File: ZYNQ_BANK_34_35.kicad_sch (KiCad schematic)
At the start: 16 parts, among them U1 XC7Z020-2CLG484I

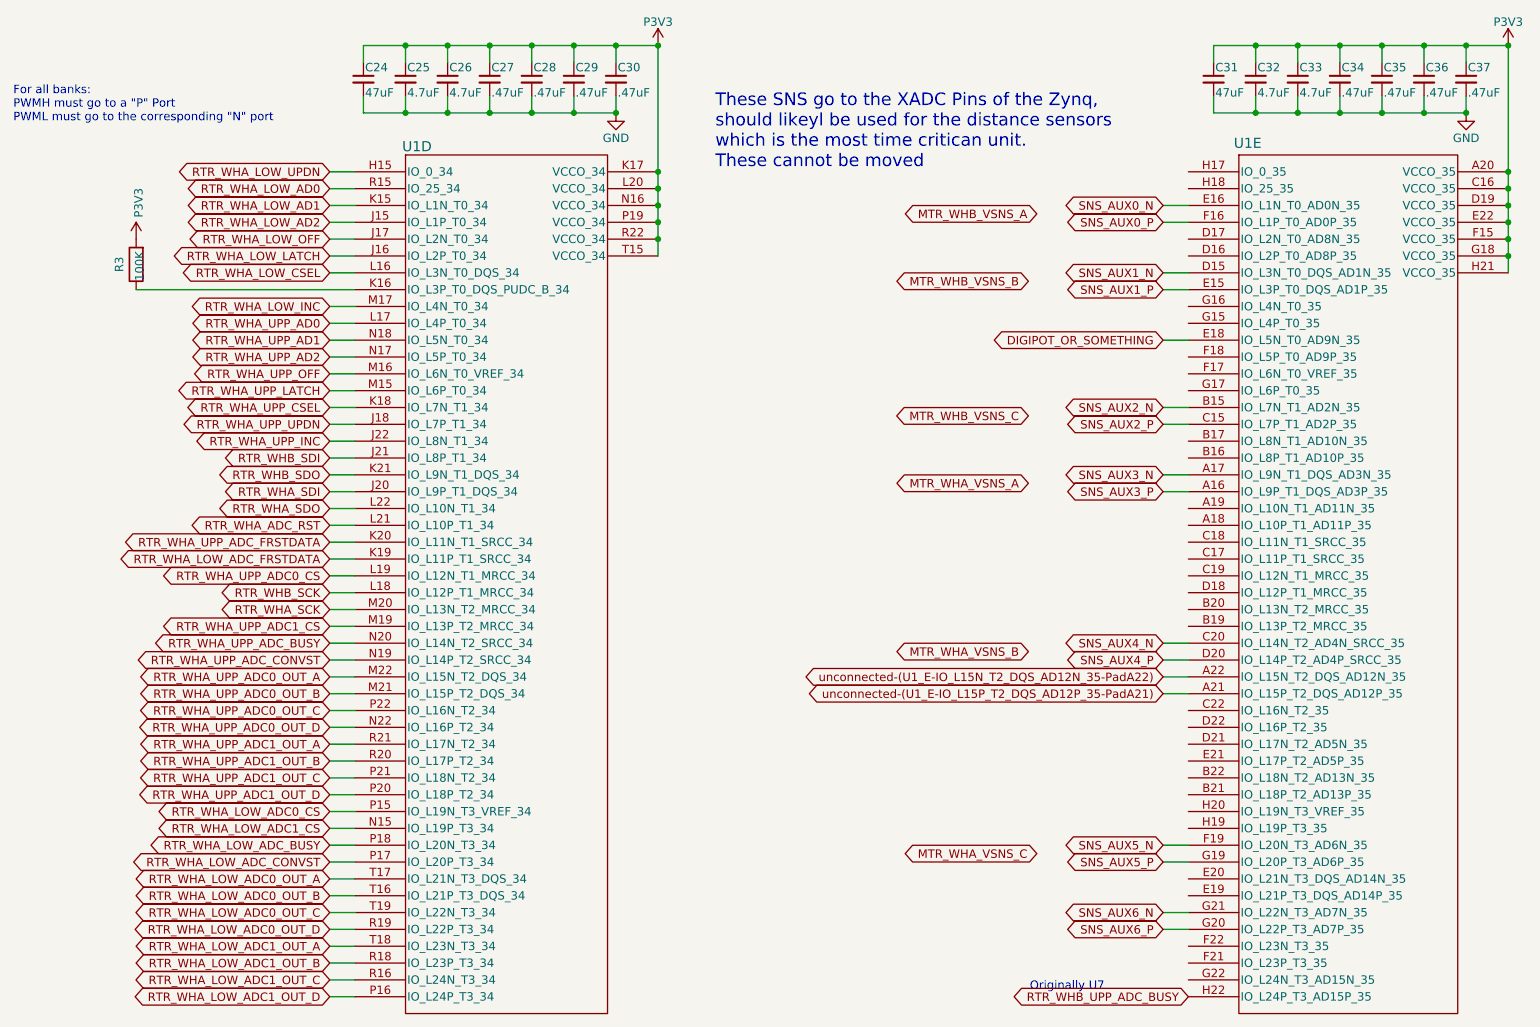
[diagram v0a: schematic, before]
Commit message: updated layouts, added motor
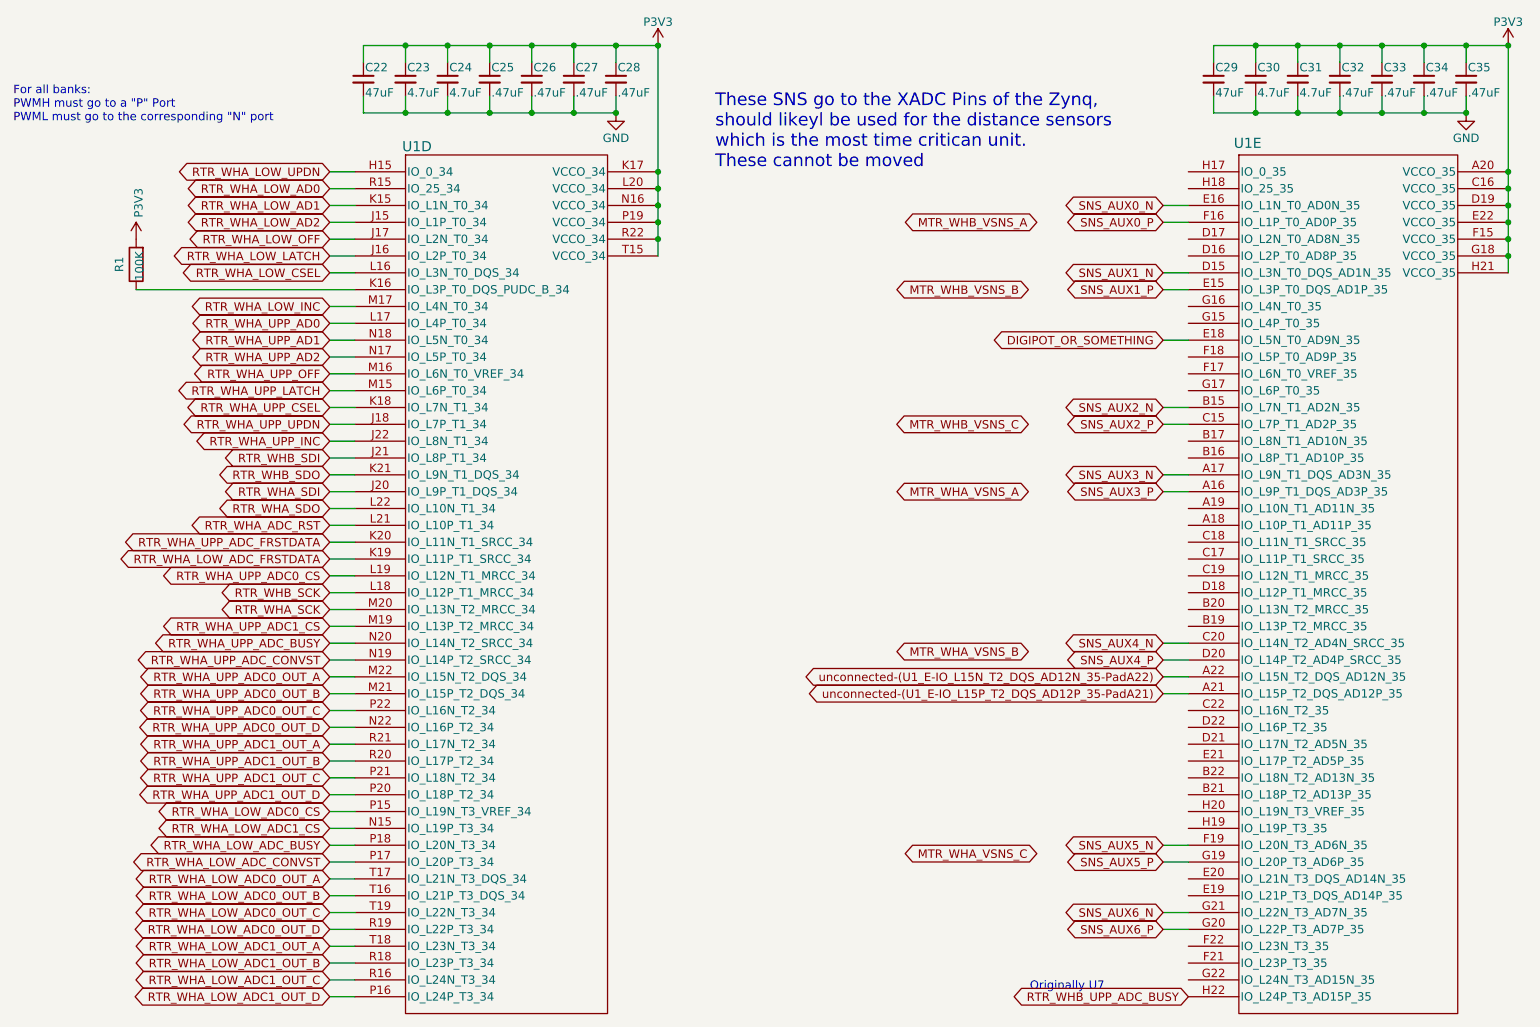
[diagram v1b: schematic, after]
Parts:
- renumbered C24 to C22, C25 to C23, C26 to C24, C27 to C25, C28 to C26, C29 to C27, C30 to C28, C31 to C29, C32 to C30, C33 to C31, C34 to C32, C35 to C33, C36 to C34, C37 to C35, R3 to R1

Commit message: Changes to layout pins
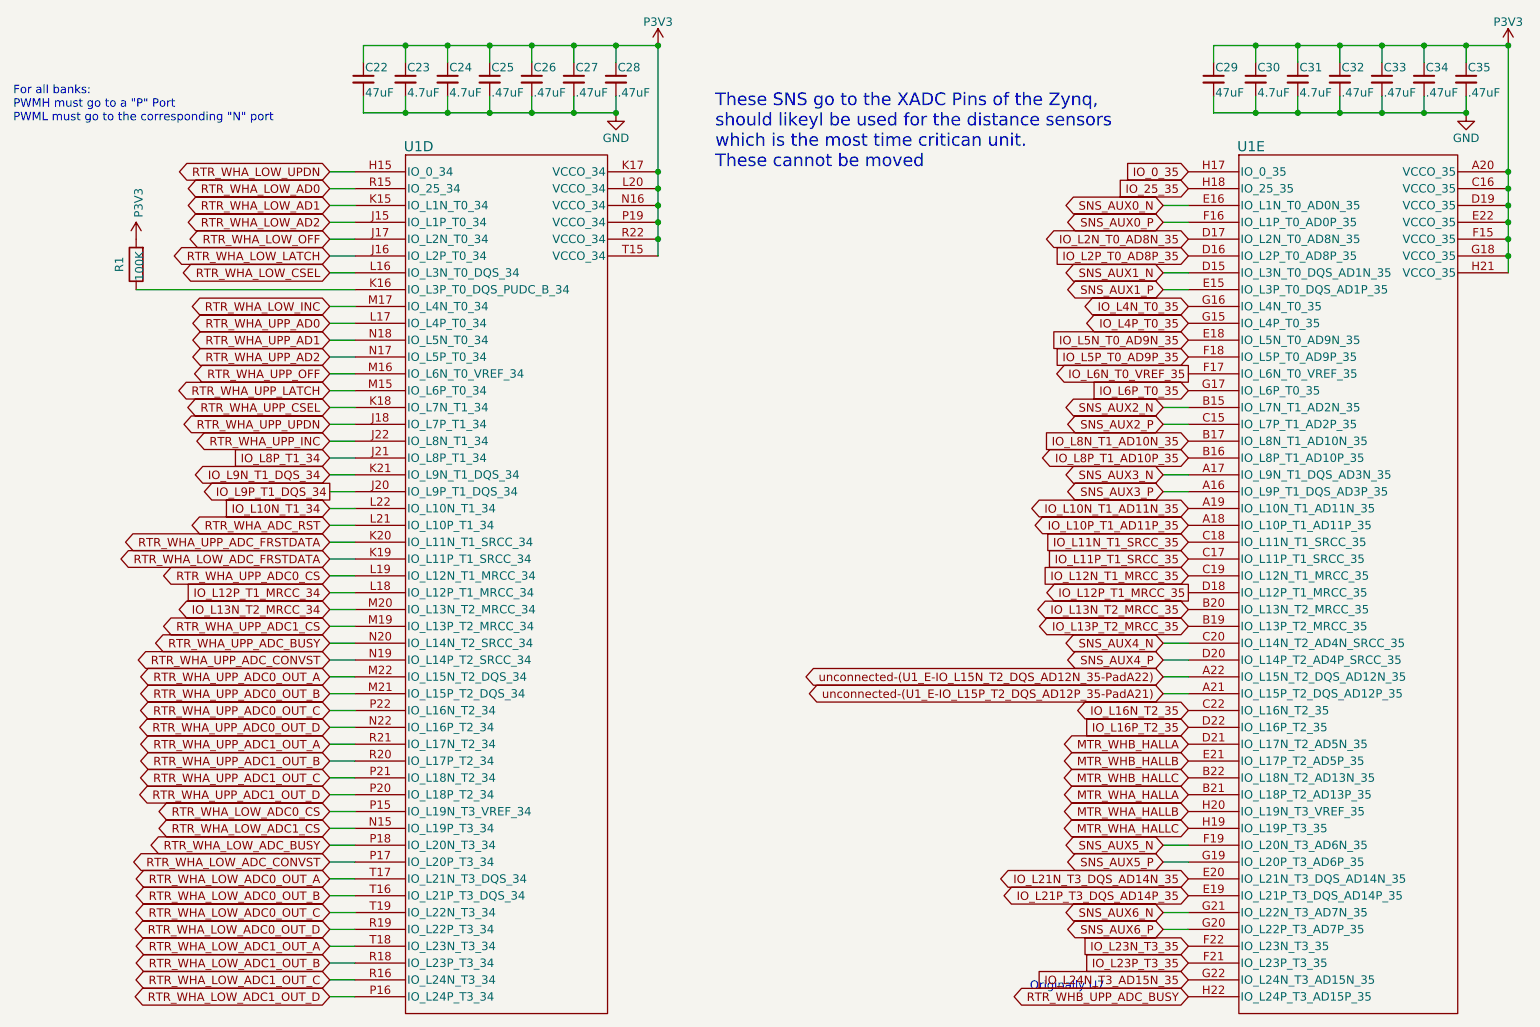
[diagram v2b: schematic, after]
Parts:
- U1: footprint DFTcustom:BGA-484_19.0x19.0mm_Layout22x22_P0.80mm_dia0.40mm -> FPGA:BGA-484_19.0x19.0mm_Layout22x22_P0.80mm_dia0.40mm
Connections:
- net IO_L10P_T1_AD11P_35: now reaches U1.A18 (IO_L10P_T1_AD11P_35)
- net IO_L10N_T1_AD11N_35: now reaches U1.A19 (IO_L10N_T1_AD11N_35)
- net IO_L8P_T1_AD10P_35: now reaches U1.B16 (IO_L8P_T1_AD10P_35)
- net IO_L8N_T1_AD10N_35: now reaches U1.B17 (IO_L8N_T1_AD10N_35)
- net IO_L13P_T2_MRCC_35: now reaches U1.B19 (IO_L13P_T2_MRCC_35)
- net IO_L13N_T2_MRCC_35: now reaches U1.B20 (IO_L13N_T2_MRCC_35)
- net MTR_WHA_HALLA: now reaches U1.B21 (IO_L18P_T2_AD13P_35)
- net MTR_WHB_HALLC: now reaches U1.B22 (IO_L18N_T2_AD13N_35)
- net IO_L11P_T1_SRCC_35: now reaches U1.C17 (IO_L11P_T1_SRCC_35)
- net IO_L11N_T1_SRCC_35: now reaches U1.C18 (IO_L11N_T1_SRCC_35)
- net IO_L12N_T1_MRCC_35: now reaches U1.C19 (IO_L12N_T1_MRCC_35)
- net IO_L16N_T2_35: now reaches U1.C22 (IO_L16N_T2_35)
- net IO_L2P_T0_AD8P_35: now reaches U1.D16 (IO_L2P_T0_AD8P_35)
- net IO_L2N_T0_AD8N_35: now reaches U1.D17 (IO_L2N_T0_AD8N_35)
- net IO_L12P_T1_MRCC_35: now reaches U1.D18 (IO_L12P_T1_MRCC_35)
- net MTR_WHB_HALLA: now reaches U1.D21 (IO_L17N_T2_AD5N_35)
- net IO_L16P_T2_35: now reaches U1.D22 (IO_L16P_T2_35)
- net IO_L21P_T3_DQS_AD14P_35: now reaches U1.E19 (IO_L21P_T3_DQS_AD14P_35)
- net IO_L21N_T3_DQS_AD14N_35: now reaches U1.E20 (IO_L21N_T3_DQS_AD14N_35)
- net MTR_WHB_HALLB: now reaches U1.E21 (IO_L17P_T2_AD5P_35)
- net IO_L6N_T0_VREF_35: now reaches U1.F17 (IO_L6N_T0_VREF_35)
- net IO_L5P_T0_AD9P_35: now reaches U1.F18 (IO_L5P_T0_AD9P_35)
- net IO_L23P_T3_35: now reaches U1.F21 (IO_L23P_T3_35)
- net IO_L23N_T3_35: now reaches U1.F22 (IO_L23N_T3_35)
- net IO_L4P_T0_35: now reaches U1.G15 (IO_L4P_T0_35)
- net IO_L4N_T0_35: now reaches U1.G16 (IO_L4N_T0_35)
- net IO_L6P_T0_35: now reaches U1.G17 (IO_L6P_T0_35)
- net IO_L24N_T3_AD15N_35: now reaches U1.G22 (IO_L24N_T3_AD15N_35)
- net IO_0_35: now reaches U1.H17 (IO_0_35)
- net IO_25_35: now reaches U1.H18 (IO_25_35)
- net MTR_WHA_HALLC: now reaches U1.H19 (IO_L19P_T3_35)
- net MTR_WHA_HALLB: now reaches U1.H20 (IO_L19N_T3_VREF_35)
- net DIGIPOT_OR_SOMETHING renamed IO_L5N_T0_AD9N_35
- net RTR_WHA_SCK renamed IO_L13N_T2_MRCC_34
- net RTR_WHA_SDI renamed IO_L9P_T1_DQS_34
- net RTR_WHA_SDO renamed IO_L10N_T1_34
- net RTR_WHB_SCK renamed IO_L12P_T1_MRCC_34
- net RTR_WHB_SDI renamed IO_L8P_T1_34
- net RTR_WHB_SDO renamed IO_L9N_T1_DQS_34
